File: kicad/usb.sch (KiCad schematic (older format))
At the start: 4 parts, among them P3 USB_OTG, U5 USBLC6-2

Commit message: Added footprints for most major components
We are missing almost all passives
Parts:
- added C27: C, symbol C
- added R36: R, symbol R
- P3: footprint (none) -> simple-led-watch:AMP-10104110-USB; Part No. (none) -> 609-4052-1-ND
- U5: footprint (none) -> simple-led-watch:SOT-666
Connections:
- net GND: now also C27.2, R36.2
- net at P3.6 (shield): now also C27.1, R36.1
- no-connect marks 2 -> 1
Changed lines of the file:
@@
 F 0 "P3" H 4075 3175 50  0000 C CNN
 F 1 "USB_OTG" H 3750 3500 50  0000 C CNN
-F 2 "" V 3700 3200 50  0000 C CNN
+F 2 "simple-led-watch:AMP-10104110-USB" V 3700 3200 50  0001 C CNN
 F 3 "" V 3700 3200 50  0000 C CNN
+F 4 "609-4052-1-ND" H 3750 3300 60  0001 C CNN "Part No."
 	1    3750 3300
 	0    -1   1    0
 $EndComp
-NoConn ~ 3650 3700
 $Comp
-L GND #PWR38
+L GND #PWR036
 U 1 1 57FA8252
 P 4200 3650
-F 0 "#PWR38" H 4200 3400 50  0001 C CNN
+F 0 "#PWR036" H 4200 3400 50  0001 C CNN
 F 1 "GND" H 4200 3500 50  0000 C CNN
 F 2 "" H 4200 3650 50  0000 C CNN
@@
 F 0 "U5" H 6300 3450 60  0000 C CNN
 F 1 "USBLC6-2" H 6300 4350 60  0000 C CNN
-F 2 "" H 6300 3900 60  0001 C CNN
+F 2 "simple-led-watch:SOT-666" H 6300 3900 60  0001 C CNN
 F 3 "" H 6300 3900 60  0001 C CNN
 F 4 "497-5026-1-ND" H 6300 3900 60  0001 C CNN "Part No."
@@
 $EndComp
 $Comp
-L GND #PWR39
+L GND #PWR037
 U 1 1 57FA84E6
 P 5700 4400
-F 0 "#PWR39" H 5700 4150 50  0001 C CNN
+F 0 "#PWR037" H 5700 4150 50  0001 C CNN
 F 1 "GND" H 5700 4250 50  0000 C CNN
 F 2 "" H 5700 4400 50  0000 C CNN
@@
 $EndComp
 $Comp
-L GND #PWR36
+L GND #PWR038
 U 1 1 57FA8E78
 P 8700 3600
-F 0 "#PWR36" H 8700 3350 50  0001 C CNN
+F 0 "#PWR038" H 8700 3350 50  0001 C CNN
 F 1 "GND" H 8700 3450 50  0000 C CNN
 F 2 "" H 8700 3600 50  0000 C CNN
@@
 Connection ~ 9000 3100
 $Comp
-L GND #PWR37
+L GND #PWR039
 U 1 1 57FA8F18
 P 9000 3600
-F 0 "#PWR37" H 9000 3350 50  0001 C CNN
+F 0 "#PWR039" H 9000 3350 50  0001 C CNN
 F 1 "GND" H 9000 3450 50  0000 C CNN
 F 2 "" H 9000 3600 50  0000 C CNN
@@
 Wire Wire Line
 	9000 3600 9000 3500
+$Comp
+L R R36
+U 1 1 5805F39C
+P 3400 4050
+F 0 "R36" V 3480 4050 50  0000 C CNN
+F 1 "R" V 3400 4050 50  0000 C CNN
+F 2 "" V 3330 4050 50  0000 C CNN
+F 3 "" H 3400 4050 50  0000 C CNN
+	1    3400 4050
+	1    0    0    -1
+$EndComp
+$Comp
+L C C27
+U 1 1 5805F3E3
+P 3650 4050
+F 0 "C27" H 3675 4150 50  0000 L CNN
+F 1 "C" H 3675 3950 50  0000 L CNN
+F 2 "" H 3688 3900 50  0000 C CNN
+F 3 "" H 3650 4050 50  0000 C CNN
+	1    3650 4050
+	1    0    0    -1
+$EndComp
+Wire Wire Line
+	3650 3700 3650 3900
+Wire Wire Line
+	3650 3800 3400 3800
+Wire Wire Line
+	3400 3800 3400 3900
+Connection ~ 3650 3800
+Wire Wire Line
+	3400 4200 3400 4300
+Wire Wire Line
+	3400 4300 3650 4300
+Wire Wire Line
+	3650 4200 3650 4400
+$Comp
+L GND #PWR040
+U 1 1 5805F4FD
+P 3650 4400
+F 0 "#PWR040" H 3650 4150 50  0001 C CNN
+F 1 "GND" H 3650 4250 50  0000 C CNN
+F 2 "" H 3650 4400 50  0000 C CNN
+F 3 "" H 3650 4400 50  0000 C CNN
+	1    3650 4400
+	1    0    0    -1
+$EndComp
+Connection ~ 3650 4300
 $EndSCHEMATC

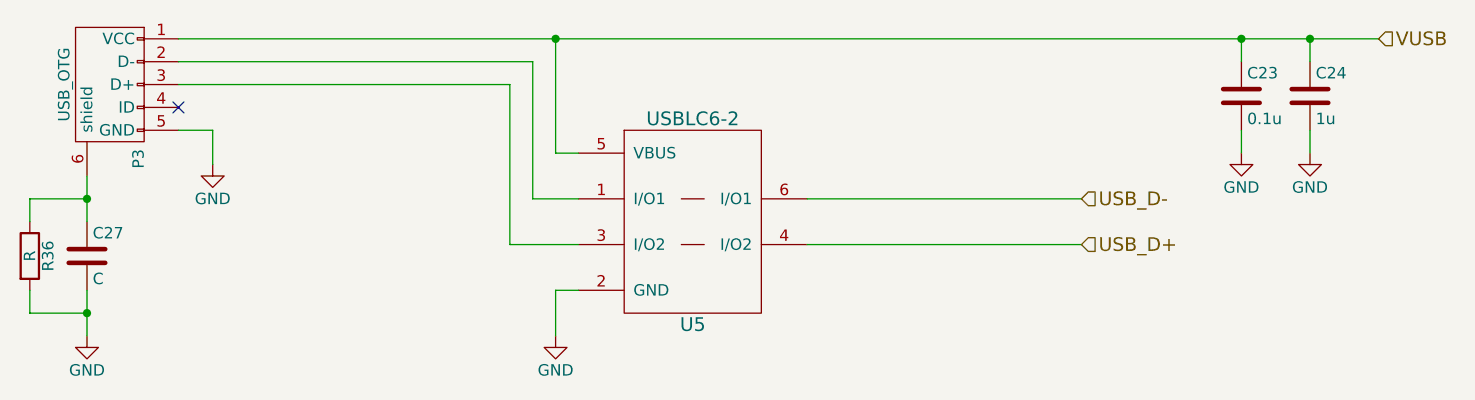
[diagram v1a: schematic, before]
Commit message: Completed initial placement of major components
The passives are causing trouble. We need to eliminate every pullup
possible.
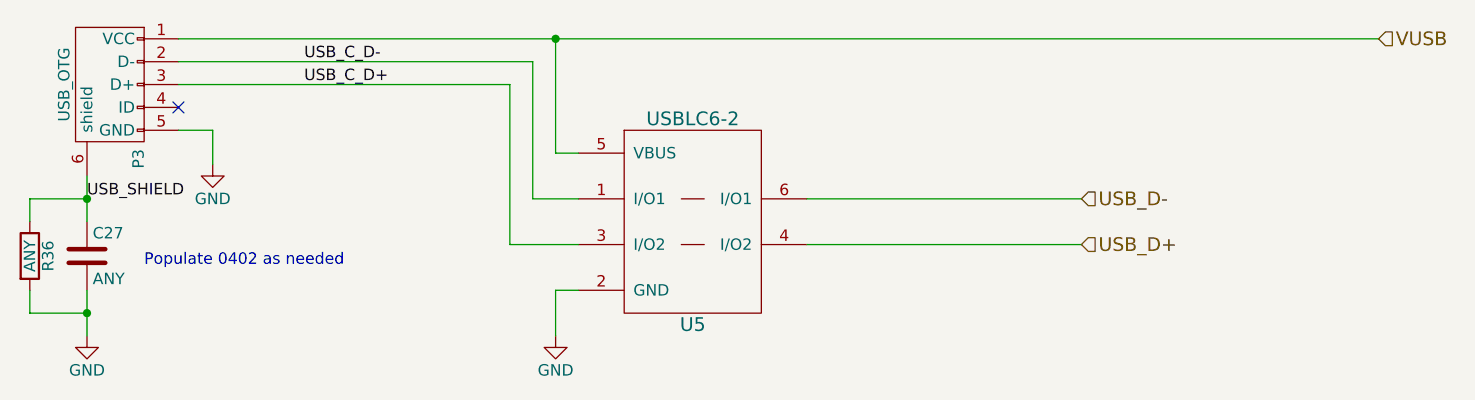
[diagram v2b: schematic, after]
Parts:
- removed C23: 0.1u, symbol C
- removed C24: 1u, symbol C
- C27: value C -> ANY; footprint (none) -> Capacitors_SMD:C_0402
- R36: value R -> ANY; footprint (none) -> Resistors_SMD:R_0402
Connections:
- net USB_C_D-: now reaches P3.2 (D-), U5.1 (I/O1)
- net USB_C_D+: now reaches P3.3 (D+), U5.3 (I/O2)
- net USB_SHIELD: now reaches C27.1, P3.6 (shield), R36.1
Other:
- note added: "Populate 0402 as needed"
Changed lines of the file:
@@
 	8000 4000 6800 4000
-$Comp
-L C C23
-U 1 1 57FA8DB8
-P 8700 3350
-F 0 "C23" H 8725 3450 50  0000 L CNN
-F 1 "0.1u" H 8725 3250 50  0000 L CNN
-F 2 "" H 8738 3200 50  0000 C CNN
-F 3 "" H 8700 3350 50  0000 C CNN
-	1    8700 3350
-	1    0    0    -1
-$EndComp
-$Comp
-L GND #PWR038
-U 1 1 57FA8E78
-P 8700 3600
-F 0 "#PWR038" H 8700 3350 50  0001 C CNN
-F 1 "GND" H 8700 3450 50  0000 C CNN
-F 2 "" H 8700 3600 50  0000 C CNN
-F 3 "" H 8700 3600 50  0000 C CNN
-	1    8700 3600
-	1    0    0    -1
-$EndComp
-Wire Wire Line
-	8700 3600 8700 3500
-Wire Wire Line
-	8700 3200 8700 3100
-Connection ~ 8700 3100
-$Comp
-L C C24
-U 1 1 57FA8ED8
-P 9000 3350
-F 0 "C24" H 9025 3450 50  0000 L CNN
-F 1 "1u" H 9025 3250 50  0000 L CNN
-F 2 "" H 9038 3200 50  0000 C CNN
-F 3 "" H 9000 3350 50  0000 C CNN
-	1    9000 3350
-	1    0    0    -1
-$EndComp
-Wire Wire Line
-	9000 3200 9000 3100
-Connection ~ 9000 3100
-$Comp
-L GND #PWR039
-U 1 1 57FA8F18
-P 9000 3600
-F 0 "#PWR039" H 9000 3350 50  0001 C CNN
-F 1 "GND" H 9000 3450 50  0000 C CNN
-F 2 "" H 9000 3600 50  0000 C CNN
-F 3 "" H 9000 3600 50  0000 C CNN
-	1    9000 3600
-	1    0    0    -1
-$EndComp
-Wire Wire Line
-	9000 3600 9000 3500
 $Comp
 L R R36
@@
 P 3400 4050
 F 0 "R36" V 3480 4050 50  0000 C CNN
-F 1 "R" V 3400 4050 50  0000 C CNN
-F 2 "" V 3330 4050 50  0000 C CNN
+F 1 "ANY" V 3400 4050 50  0000 C CNN
+F 2 "Resistors_SMD:R_0402" V 3330 4050 50  0001 C CNN
 F 3 "" H 3400 4050 50  0000 C CNN
 	1    3400 4050
@@
 P 3650 4050
 F 0 "C27" H 3675 4150 50  0000 L CNN
-F 1 "C" H 3675 3950 50  0000 L CNN
-F 2 "" H 3688 3900 50  0000 C CNN
+F 1 "ANY" H 3675 3950 50  0000 L CNN
+F 2 "Capacitors_SMD:C_0402" H 3688 3900 50  0001 C CNN
 F 3 "" H 3650 4050 50  0000 C CNN
 	1    3650 4050
@@
 	3650 4200 3650 4400
 $Comp
-L GND #PWR040
+L GND #PWR038
 U 1 1 5805F4FD
 P 3650 4400
-F 0 "#PWR040" H 3650 4150 50  0001 C CNN
+F 0 "#PWR038" H 3650 4150 50  0001 C CNN
 F 1 "GND" H 3650 4250 50  0000 C CNN
 F 2 "" H 3650 4400 50  0000 C CNN
@@
 $EndComp
 Connection ~ 3650 4300
+Text Notes 3900 4100 0    50   ~ 0
+Populate 0402 as needed
+Text Label 4600 3200 0    50   ~ 0
+USB_C_D-
+Text Label 4600 3300 0    50   ~ 0
+USB_C_D+
+Text Label 3650 3800 0    50   ~ 0
+USB_SHIELD
 $EndSCHEMATC

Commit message: Upgrade to latest kicad, add some measurements
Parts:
- P3: symbol USB_OTG -> USB_OTG-RESCUE-simple-led-watch
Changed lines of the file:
@@
 EESchema Schematic File Version 2
+LIBS:simple-led-watch-rescue
 LIBS:power
 LIBS:device
@@
 $EndDescr
 $Comp
-L USB_OTG P3
+L USB_OTG-RESCUE-simple-led-watch P3
 U 1 1 57FA80BD
 P 3750 3300
+AR Path="/57FA80BD" Ref="P3"  Part="1"
+AR Path="/57FA8096/57FA80BD" Ref="P3"  Part="1"
 F 0 "P3" H 4075 3175 50  0000 C CNN
 F 1 "USB_OTG" H 3750 3500 50  0000 C CNN
